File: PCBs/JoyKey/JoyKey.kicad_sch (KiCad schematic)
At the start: 5 parts, among them J1 OLED_DISPLAY, J3 Testpad wire hole1, U3 XIAO-RP2040-DIP

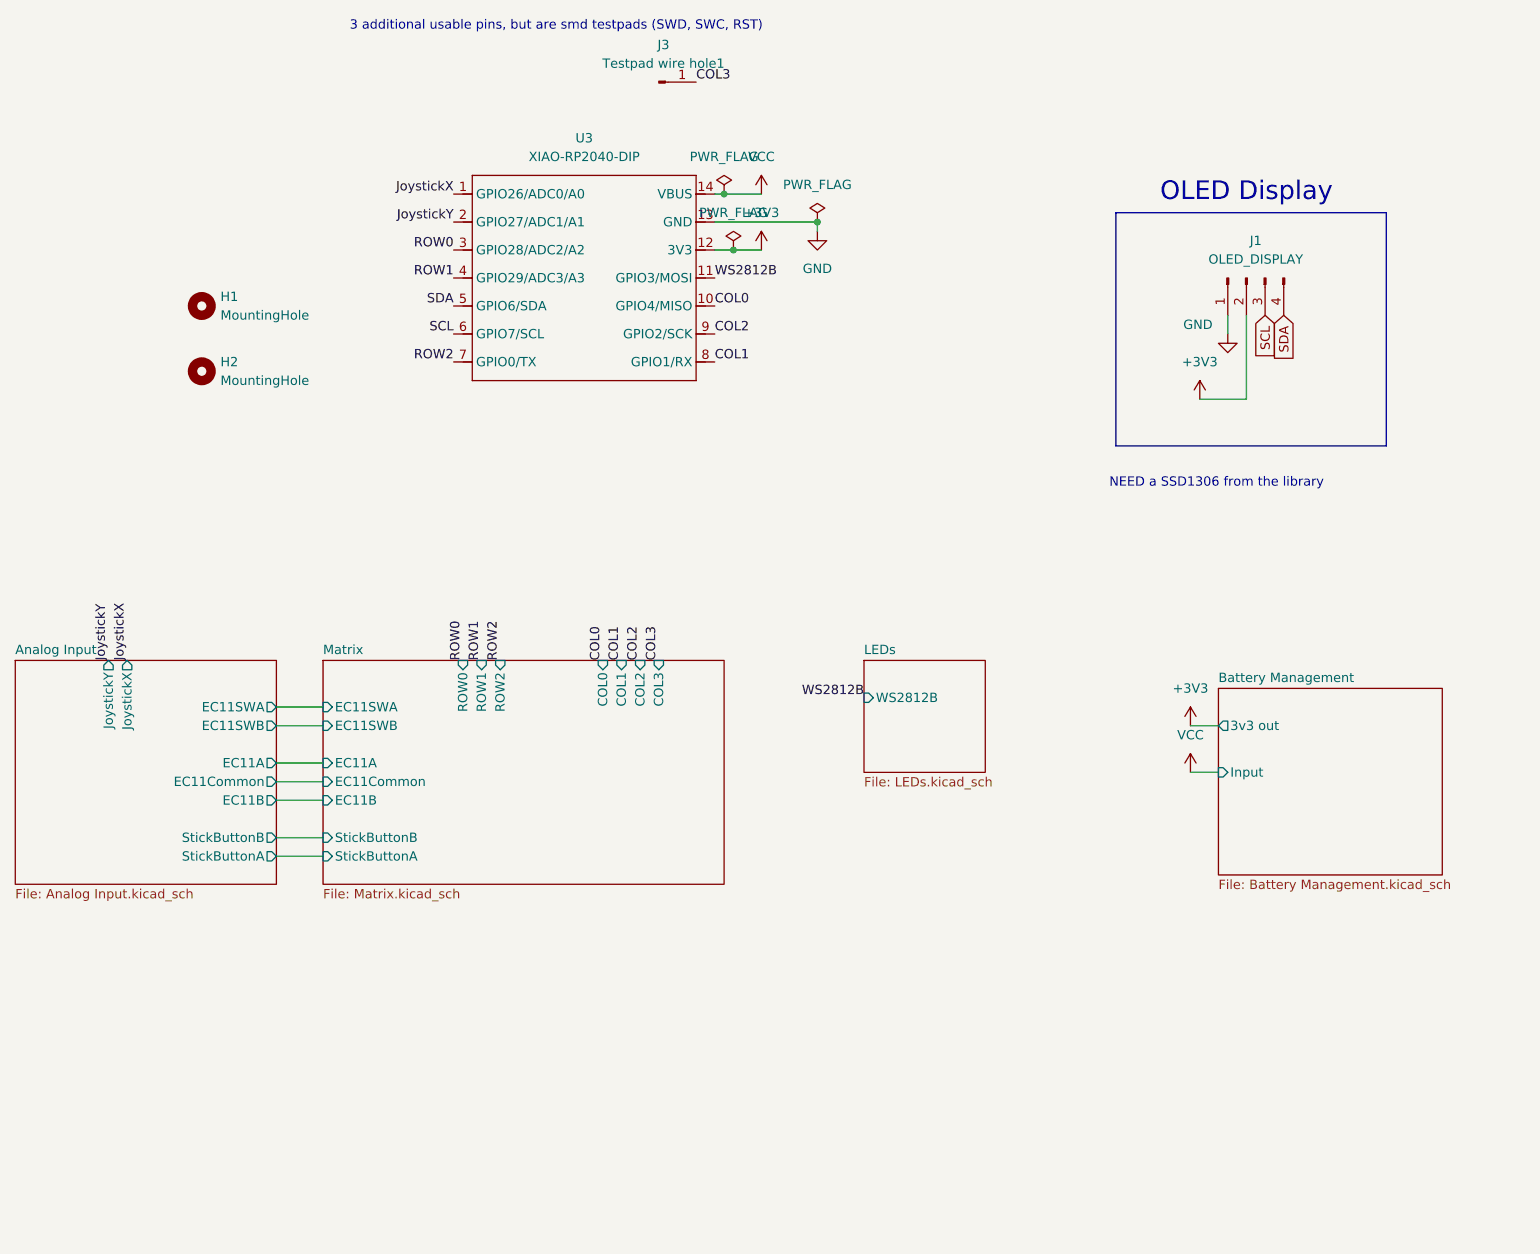
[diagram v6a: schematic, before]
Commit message: Added Accel and Gyro sensor
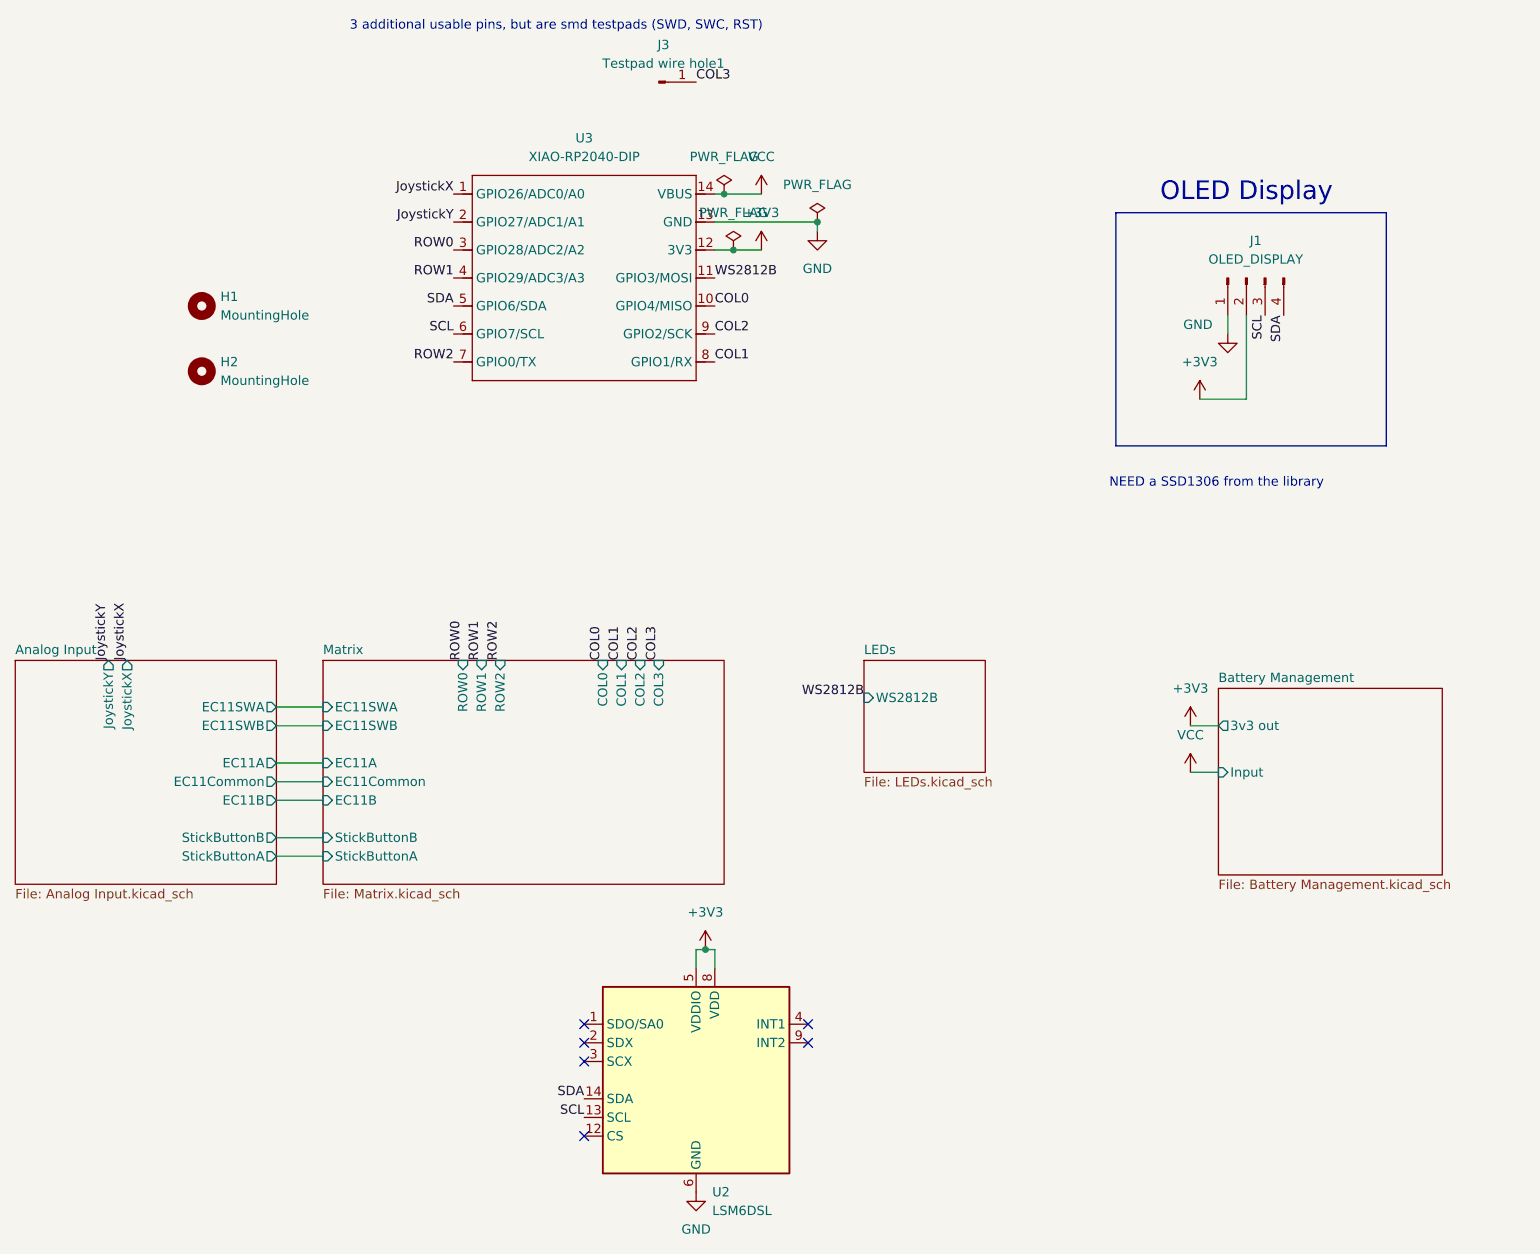
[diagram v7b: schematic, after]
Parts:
- added U2: LSM6DSL, Package_LGA:LGA-14_3x2.5mm_P0.5mm_LayoutBorder3x4y, symbol Sensor_Motion:LSM6DSL
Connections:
- net +3V3: now also U2.5 (VDDIO), U2.8 (VDD)
- net GND: now also U2.6 (GND), U2.7 (GND)
- net SCL: now also U2.13 (SCL)
- net SDA: now also U2.14 (SDA)
- no-connect marks 0 -> 6

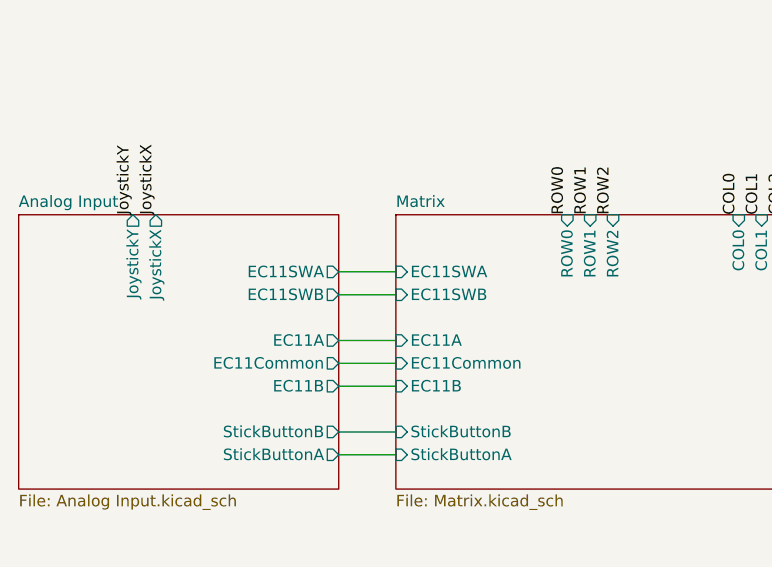
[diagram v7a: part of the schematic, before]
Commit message: Switched encoder to Alps EC12
I wanted something shorter and that didn't have a metal screw post. I do loose out on the switch though, which I've exposed via a separate header
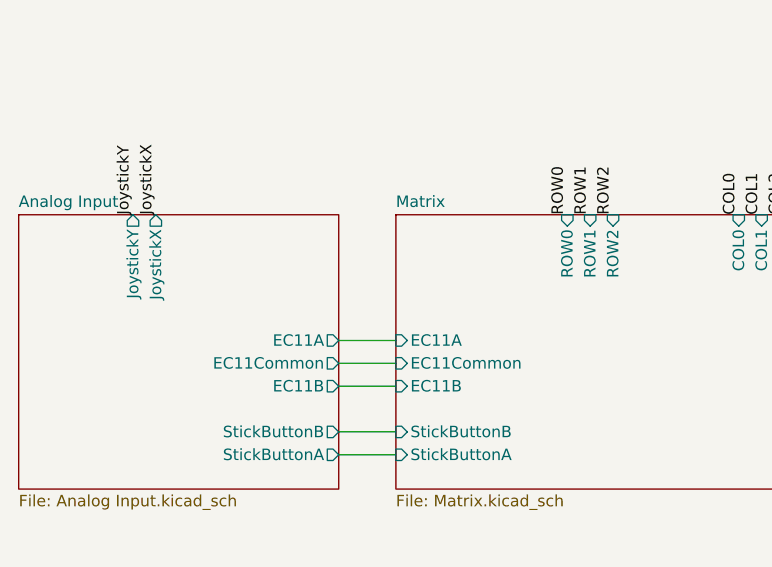
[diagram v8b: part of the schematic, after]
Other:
- sheet Analog Input ports: added none; removed EC11SWA, EC11SWB
- sheet Matrix ports: added none; removed EC11SWA, EC11SWB
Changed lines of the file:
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@@
-	(wire
-		(pts
-			(xy 78.74 110.49) (xy 85.09 110.49)
-		)
-		(stroke
-			(width 0)
-			(type default)
-		)
-	)
 	(wire
 		(pts
@@
 		(pts
 			(xy 138.43 40.64) (xy 139.7 40.64)
-		)
-		(stroke
-			(width 0)
-			(type default)
-		)
-	)
-	(wire
-		(pts
-			(xy 78.74 113.03) (xy 85.09 113.03)
 		)
 		(stroke
@@
 			)
 		)
-		(pin "EC11SWB" input
-			(at 85.09 113.03 180)
-			(effects
-				(font
-					(size 1.27 1.27)
-				)
-				(justify left)
-			)
-		)
-		(pin "EC11SWA" input
-			(at 85.09 110.49 180)
-			(effects
-				(font
-					(size 1.27 1.27)
-				)
-				(justify left)
-			)
-		)
 		(pin "StickButtonB" input
 			(at 85.09 128.27 180)
@@
 			(effects
 				(font
-					(size 1.27 1.27)
-				)
-				(justify right)
-			)
-		)
-		(pin "EC11SWB" output
-			(at 78.74 113.03 0)
-			(effects
-				(font
-					(size 1.27 1.27)
-				)
-				(justify right)
-			)
-		)
-		(pin "EC11SWA" output
-			(at 78.74 110.49 0)
-			(effects
-				(font
